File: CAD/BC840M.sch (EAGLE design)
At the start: 34 parts, among them J1 SM02B-SRSS-TB(LF)(SN), U2 BC840M, U3 LP5907MFX-3.3/NOPB, U4 LP5907MFX-3.3/NOPB, U5 ADS131M08IPBS, X1 ABM3B-8.000MHZ-B2-T, X2 FC-12M

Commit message: updated
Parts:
- removed JP4, JP5: (no value), pinhead+:PINHD-2X10SMT
- added C16, C17, C20, C21, C24, C25, C28, C29: 0.1pF, standardparts:CAPACITOR.0603
- added JP2, JP3: (no value), pinhead+:PINHD-2X10SMT
- added R10, R11, R12, R13, R14, R15, R16, R17, R18, R19, R20, R21, R6, R7, R8, R9: 1GOhm, standardparts:RESISTOR.0603
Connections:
- removed net N$2: U2.H4/VSS, U2.H5/VSS, U2.H6/VSS, U2.H7/VSS
- removed net N$3: U2.F5/VDD
- removed net N$4: U2.G4/VSS, U2.G5/VSS, U2.G6/VSS
- removed net N$46: U2.F7/P001
- removed net N$47: U2.F6/P000
- removed net N$5: U2.G0/VSS
- removed net N$8: U2.A5/D-
- removed net N$9: U2.A4/D+
- new net 0NIN: C16.2, R8.2, U5.AN0N
- new net 0PIN: C16.1, R6.2, U5.AN0P
- new net 1NIN: C17.2, R9.2, U5.AN1N
- new net 1PIN: C17.1, R7.2, U5.AN1P
- new net 2NIN: C20.2, R12.2, U5.AIN2N
- new net 2PIN: C20.1, R10.2, U5.AIN2P
- new net 3NIN: C21.2, R13.2, U5.AIN3N
- new net 3PIN: C21.1, R11.2, U5.AIN3P
- new net 4NIN: C24.2, R16.2, U5.AIN4N
- new net 4PIN: C24.1, R14.2, U5.AIN4P
- new net 5NIN: C25.2, R17.2, U5.AIN5N
- new net 5PIN: C25.1, R15.2, U5.AIN5P
- new net 6NIN: C28.2, R20.2, U5.AIN6N
- new net 6PIN: C28.1, R18.2, U5.AIN6P
- new net 7NIN: C29.2, R21.2, U5.AIN7N
- new net 7PIN: C29.1, R19.2, U5.AIN7P
- net 0N: now also JP1.2, R8.1; no longer U5.AN0N
- net 0P: now also JP1.1, R6.1; no longer U5.AN0P
- net 1N: now also JP1.4, R9.1; no longer U5.AN1N
- net 1P: now also JP1.3, R7.1; no longer U5.AN1P
- net 2N: now also JP1.6, R12.1; no longer U5.AIN2N
- net 2P: now also JP1.5, R10.1; no longer U5.AIN2P
- net 3N: now also JP1.8, R13.1; no longer U5.AIN3N
- net 3P: now also JP1.7, R11.1; no longer U5.AIN3P
- net 4N: now also JP1.10, R16.1; no longer U5.AIN4N
- net 4P: now also JP1.9, R14.1; no longer U5.AIN4P
- net 5N: now also JP1.12, R17.1; no longer U5.AIN5N
- net 5P: now also JP1.11, R15.1; no longer U5.AIN5P
- net 6N: now also JP1.14, R20.1; no longer U5.AIN6N
- net 6P: now also JP1.13, R18.1; no longer U5.AIN6P
- net 7N: now also JP1.16, R21.1; no longer U5.AIN7N
- net 7P: now also JP1.15, R19.1; no longer U5.AIN7P
- net D+: now also U2.A4/D+
- net D-: now also U2.A5/D-
- net GND: now also U2.G0/VSS, U2.G4/VSS, U2.G5/VSS, U2.G6/VSS, U2.H4/VSS, U2.H5/VSS, U2.H6/VSS, U2.H7/VSS
- net VDD: now also U2.F5/VDD
- net XTAL1_1: now also U2.F6/P000
- net XTAL2_1: now also U2.F7/P001
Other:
- note added: "Battery Charger/Switcher System (See BQ2407X datasheet)"
- note removed: "Battery Charger/Switcher System (See LOLIN32 Schematic)"

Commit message: updated
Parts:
- C16, C17, C20, C21, C24, C25, C28, C29: value 0.1pF -> 10pF
- R10, R11, R12, R13, R14, R15, R16, R17, R18, R19, R20, R21, R6, R7, R8, R9: value 1GOhm -> 10MOhm
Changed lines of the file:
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@@
 <part name="R5" library="standardparts" deviceset="RESISTOR" device=".0201" value="3.3kΩ"/>
 <part name="SUPPLY1" library="supply2" library_urn="urn:adsk.eagle:library:372" deviceset="GND" device=""/>
-<part name="C16" library="standardparts" deviceset="CAPACITOR" device=".0603" value="0.1pF"/>
-<part name="R6" library="standardparts" deviceset="RESISTOR" device=".0603" value="1GOhm"/>
-<part name="C17" library="standardparts" deviceset="CAPACITOR" device=".0603" value="0.1pF"/>
-<part name="R7" library="standardparts" deviceset="RESISTOR" device=".0603" value="1GOhm"/>
-<part name="R8" library="standardparts" deviceset="RESISTOR" device=".0603" value="1GOhm"/>
-<part name="R9" library="standardparts" deviceset="RESISTOR" device=".0603" value="1GOhm"/>
-<part name="C20" library="standardparts" deviceset="CAPACITOR" device=".0603" value="0.1pF"/>
-<part name="R10" library="standardparts" deviceset="RESISTOR" device=".0603" value="1GOhm"/>
-<part name="C21" library="standardparts" deviceset="CAPACITOR" device=".0603" value="0.1pF"/>
-<part name="R11" library="standardparts" deviceset="RESISTOR" device=".0603" value="1GOhm"/>
-<part name="R12" library="standardparts" deviceset="RESISTOR" device=".0603" value="1GOhm"/>
-<part name="R13" library="standardparts" deviceset="RESISTOR" device=".0603" value="1GOhm"/>
-<part name="C24" library="standardparts" deviceset="CAPACITOR" device=".0603" value="0.1pF"/>
-<part name="R14" library="standardparts" deviceset="RESISTOR" device=".0603" value="1GOhm"/>
-<part name="C25" library="standardparts" deviceset="CAPACITOR" device=".0603" value="0.1pF"/>
-<part name="R15" library="standardparts" deviceset="RESISTOR" device=".0603" value="1GOhm"/>
-<part name="R16" library="standardparts" deviceset="RESISTOR" device=".0603" value="1GOhm"/>
-<part name="R17" library="standardparts" deviceset="RESISTOR" device=".0603" value="1GOhm"/>
-<part name="C28" library="standardparts" deviceset="CAPACITOR" device=".0603" value="0.1pF"/>
-<part name="R18" library="standardparts" deviceset="RESISTOR" device=".0603" value="1GOhm"/>
-<part name="C29" library="standardparts" deviceset="CAPACITOR" device=".0603" value="0.1pF"/>
-<part name="R19" library="standardparts" deviceset="RESISTOR" device=".0603" value="1GOhm"/>
-<part name="R20" library="standardparts" deviceset="RESISTOR" device=".0603" value="1GOhm"/>
-<part name="R21" library="standardparts" deviceset="RESISTOR" device=".0603" value="1GOhm"/>
+<part name="C16" library="standardparts" deviceset="CAPACITOR" device=".0603" value="10pF"/>
+<part name="R6" library="standardparts" deviceset="RESISTOR" device=".0603" value="10MOhm"/>
+<part name="C17" library="standardparts" deviceset="CAPACITOR" device=".0603" value="10pF"/>
+<part name="R7" library="standardparts" deviceset="RESISTOR" device=".0603" value="10MOhm"/>
+<part name="R8" library="standardparts" deviceset="RESISTOR" device=".0603" value="10MOhm"/>
+<part name="R9" library="standardparts" deviceset="RESISTOR" device=".0603" value="10MOhm"/>
+<part name="C20" library="standardparts" deviceset="CAPACITOR" device=".0603" value="10pF"/>
+<part name="R10" library="standardparts" deviceset="RESISTOR" device=".0603" value="10MOhm"/>
+<part name="C21" library="standardparts" deviceset="CAPACITOR" device=".0603" value="10pF"/>
+<part name="R11" library="standardparts" deviceset="RESISTOR" device=".0603" value="10MOhm"/>
+<part name="R12" library="standardparts" deviceset="RESISTOR" device=".0603" value="10MOhm"/>
+<part name="R13" library="standardparts" deviceset="RESISTOR" device=".0603" value="10MOhm"/>
+<part name="C24" library="standardparts" deviceset="CAPACITOR" device=".0603" value="10pF"/>
+<part name="R14" library="standardparts" deviceset="RESISTOR" device=".0603" value="10MOhm"/>
+<part name="C25" library="standardparts" deviceset="CAPACITOR" device=".0603" value="10pF"/>
+<part name="R15" library="standardparts" deviceset="RESISTOR" device=".0603" value="10MOhm"/>
+<part name="R16" library="standardparts" deviceset="RESISTOR" device=".0603" value="10MOhm"/>
+<part name="R17" library="standardparts" deviceset="RESISTOR" device=".0603" value="10MOhm"/>
+<part name="C28" library="standardparts" deviceset="CAPACITOR" device=".0603" value="10pF"/>
+<part name="R18" library="standardparts" deviceset="RESISTOR" device=".0603" value="10MOhm"/>
+<part name="C29" library="standardparts" deviceset="CAPACITOR" device=".0603" value="10pF"/>
+<part name="R19" library="standardparts" deviceset="RESISTOR" device=".0603" value="10MOhm"/>
+<part name="R20" library="standardparts" deviceset="RESISTOR" device=".0603" value="10MOhm"/>
+<part name="R21" library="standardparts" deviceset="RESISTOR" device=".0603" value="10MOhm"/>
 <part name="SUPPLY22" library="supply2" library_urn="urn:adsk.eagle:library:372" deviceset="GND" device=""/>
 <part name="SUPPLY23" library="supply2" library_urn="urn:adsk.eagle:library:372" deviceset="GND" device=""/>

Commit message: i/o prerouting
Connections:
- net N$10 renamed SWDIO
- net N$11 renamed P104
- net N$12 renamed P101
- net N$13 renamed P25
- net N$14 renamed P19
- net N$15 renamed P17
- net N$16 renamed P22
- net N$17 renamed P15
- net N$18 renamed RESET
- net N$19 renamed VBUS
- net N$20 renamed P7
- net N$21 renamed P12
- net N$22 renamed P107
- net N$23 renamed SWDCLK
- net N$24 renamed P20
- net N$25 renamed P21
- net N$26 renamed P14
- net N$27 renamed P108
- net N$28 renamed P109
- net N$29 renamed P8
- net N$30 renamed P100
- net N$31 renamed P105
- net N$32 renamed P9
- net N$33 renamed P16
- net N$34 renamed P13
- net N$35 renamed P11
- net N$36 renamed P27
- net N$37 renamed P6
- net N$38 renamed P103
- net N$39 renamed P106
- net N$40 renamed P10
- net N$41 renamed P115
- net N$42 renamed P29
- net N$43 renamed P31
- net N$44 renamed P26
- net N$45 renamed P4
- net N$49 renamed P2
- net N$50 renamed P112
- net N$51 renamed P102
- net N$52 renamed P24
- net N$53 renamed P23
- net N$54 renamed P5
- net N$55 renamed P113
- net N$56 renamed P111
- net N$57 renamed P30
- net N$58 renamed P114
- net N$59 renamed P110
- net N$6 renamed VDDH
- net N$60 renamed P28
- net N$61 renamed P3
- net N$7 renamed DCCH

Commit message: latest
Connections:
- net N$63 renamed CE
- net N$68 renamed EN1
- net N$69 renamed EN2
- net N$72 renamed TD
- net N$74 renamed TS
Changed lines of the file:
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@@
 <grid distance="1" unitdist="mil" unit="mil" style="lines" multiple="1" display="no" altdistance="0.01" altunitdist="inch" altunit="inch"/>
 <layers>
-<layer number="1" name="Top" color="4" fill="1" visible="yes" active="no"/>
-<layer number="2" name="Route2" color="16" fill="1" visible="yes" active="no"/>
-<layer number="3" name="Route3" color="17" fill="1" visible="yes" active="no"/>
-<layer number="4" name="Route4" color="18" fill="1" visible="yes" active="no"/>
-<layer number="5" name="Route5" color="19" fill="1" visible="yes" active="no"/>
-<layer number="6" name="Route6" color="25" fill="1" visible="yes" active="no"/>
-<layer number="7" name="Route7" color="26" fill="1" visible="yes" active="no"/>
-<layer number="8" name="Route8" color="27" fill="1" visible="yes" active="no"/>
-<layer number="9" name="Route9" color="28" fill="1" visible="yes" active="no"/>
-<layer number="10" name="Route10" color="29" fill="1" visible="yes" active="no"/>
-<layer number="11" name="Route11" color="30" fill="1" visible="yes" active="no"/>
-<layer number="12" name="Route12" color="20" fill="1" visible="yes" active="no"/>
-<layer number="13" name="Route13" color="21" fill="1" visible="yes" active="no"/>
-<layer number="14" name="Route14" color="22" fill="1" visible="yes" active="no"/>
-<layer number="15" name="Route15" color="23" fill="1" visible="yes" active="no"/>
-<layer number="16" name="Bottom" color="1" fill="1" visible="yes" active="no"/>
-<layer number="17" name="Pads" color="2" fill="1" visible="yes" active="no"/>
-<layer number="18" name="Vias" color="2" fill="1" visible="yes" active="no"/>
-<layer number="19" name="Unrouted" color="6" fill="1" visible="yes" active="no"/>
-<layer number="20" name="Dimension" color="24" fill="1" visible="yes" active="no"/>
-<layer number="21" name="tPlace" color="7" fill="1" visible="yes" active="no"/>
-<layer number="22" name="bPlace" color="7" fill="1" visible="yes" active="no"/>
-<layer number="23" name="tOrigins" color="15" fill="1" visible="yes" active="no"/>
-<layer number="24" name="bOrigins" color="15" fill="1" visible="yes" active="no"/>
-<layer number="25" name="tNames" color="7" fill="1" visible="yes" active="no"/>
-<layer number="26" name="bNames" color="7" fill="1" visible="yes" active="no"/>
-<layer number="27" name="tValues" color="7" fill="1" visible="yes" active="no"/>
-<layer number="28" name="bValues" color="7" fill="1" visible="yes" active="no"/>
+<layer number="1" name="Top" color="4" fill="1" visible="no" active="no"/>
+<layer number="2" name="Route2" color="16" fill="1" visible="no" active="no"/>
+<layer number="3" name="Route3" color="17" fill="1" visible="no" active="no"/>
+<layer number="4" name="Route4" color="18" fill="1" visible="no" active="no"/>
+<layer number="5" name="Route5" color="19" fill="1" visible="no" active="no"/>
+<layer number="6" name="Route6" color="25" fill="1" visible="no" active="no"/>
+<layer number="7" name="Route7" color="26" fill="1" visible="no" active="no"/>
+<layer number="8" name="Route8" color="27" fill="1" visible="no" active="no"/>
+<layer number="9" name="Route9" color="28" fill="1" visible="no" active="no"/>
+<layer number="10" name="Route10" color="29" fill="1" visible="no" active="no"/>
+<layer number="11" name="Route11" color="30" fill="1" visible="no" active="no"/>
+<layer number="12" name="Route12" color="20" fill="1" visible="no" active="no"/>
+<layer number="13" name="Route13" color="21" fill="1" visible="no" active="no"/>
+<layer number="14" name="Route14" color="22" fill="1" visible="no" active="no"/>
+<layer number="15" name="Route15" color="23" fill="1" visible="no" active="no"/>
+<layer number="16" name="Bottom" color="1" fill="1" visible="no" active="no"/>
+<layer number="17" name="Pads" color="2" fill="1" visible="no" active="no"/>
+<layer number="18" name="Vias" color="2" fill="1" visible="no" active="no"/>
+<layer number="19" name="Unrouted" color="6" fill="1" visible="no" active="no"/>
+<layer number="20" name="Dimension" color="24" fill="1" visible="no" active="no"/>
+<layer number="21" name="tPlace" color="7" fill="1" visible="no" active="no"/>
+<layer number="22" name="bPlace" color="7" fill="1" visible="no" active="no"/>
+<layer number="23" name="tOrigins" color="15" fill="1" visible="no" active="no"/>
+<layer number="24" name="bOrigins" color="15" fill="1" visible="no" active="no"/>
+<layer number="25" name="tNames" color="7" fill="1" visible="no" active="no"/>
+<layer number="26" name="bNames" color="7" fill="1" visible="no" active="no"/>
+<layer number="27" name="tValues" color="7" fill="1" visible="no" active="no"/>
+<layer number="28" name="bValues" color="7" fill="1" visible="no" active="no"/>
 <layer number="29" name="tStop" color="7" fill="3" visible="no" active="no"/>
 <layer number="30" name="bStop" color="7" fill="6" visible="no" active="no"/>
@@
 <layer number="35" name="tGlue" color="7" fill="4" visible="no" active="no"/>
 <layer number="36" name="bGlue" color="7" fill="5" visible="no" active="no"/>
-<layer number="37" name="tTest" color="7" fill="1" visible="yes" active="no"/>
-<layer number="38" name="bTest" color="7" fill="1" visible="yes" active="no"/>
+<layer number="37" name="tTest" color="7" fill="1" visible="no" active="no"/>
+<layer number="38" name="bTest" color="7" fill="1" visible="no" active="no"/>
 <layer number="39" name="tKeepout" color="4" fill="11" visible="no" active="no"/>
 <layer number="40" name="bKeepout" color="1" fill="11" visible="no" active="no"/>
@@
 <layer number="44" name="Drills" color="7" fill="1" visible="no" active="no"/>
 <layer number="45" name="Holes" color="7" fill="1" visible="no" active="no"/>
-<layer number="46" name="Milling" color="3" fill="1" visible="yes" active="no"/>
-<layer number="47" name="Measures" color="7" fill="1" visible="yes" active="no"/>
-<layer number="48" name="Document" color="7" fill="1" visible="yes" active="no"/>
-<layer number="49" name="Reference" color="7" fill="1" visible="yes" active="no"/>
-<layer number="50" name="dxf" color="7" fill="1" visible="yes" active="no"/>
-<layer number="51" name="tDocu" color="7" fill="1" visible="yes" active="no"/>
-<layer number="52" name="bDocu" color="7" fill="1" visible="yes" active="no"/>
-<layer number="53" name="tGND_GNDA" color="7" fill="9" visible="yes" active="no"/>
-<layer number="54" name="bGND_GNDA" color="1" fill="9" visible="yes" active="no"/>
-<layer number="56" name="wert" color="7" fill="1" visible="yes" active="no"/>
-<layer number="57" name="tCAD" color="7" fill="1" visible="yes" active="no"/>
-<layer number="59" name="tCarbon" color="7" fill="1" visible="yes" active="no"/>
-<layer number="60" name="bCarbon" color="7" fill="1" visible="yes" active="no"/>
+<layer number="46" name="Milling" color="3" fill="1" visible="no" active="no"/>
+<layer number="47" name="Measures" color="7" fill="1" visible="no" active="no"/>
+<layer number="48" name="Document" color="7" fill="1" visible="no" active="no"/>
+<layer number="49" name="Reference" color="7" fill="1" visible="no" active="no"/>
+<layer number="50" name="dxf" color="7" fill="1" visible="no" active="no"/>
+<layer number="51" name="tDocu" color="7" fill="1" visible="no" active="no"/>
+<layer number="52" name="bDocu" color="7" fill="1" visible="no" active="no"/>
+<layer number="53" name="tGND_GNDA" color="7" fill="9" visible="no" active="no"/>
+<layer number="54" name="bGND_GNDA" color="1" fill="9" visible="no" active="no"/>
+<layer number="56" name="wert" color="7" fill="1" visible="no" active="no"/>
+<layer number="57" name="tCAD" color="7" fill="1" visible="no" active="no"/>
+<layer number="59" name="tCarbon" color="7" fill="1" visible="no" active="no"/>
+<layer number="60" name="bCarbon" color="7" fill="1" visible="no" active="no"/>
 <layer number="88" name="SimResults" color="9" fill="1" visible="yes" active="yes"/>
 <layer number="89" name="SimProbes" color="9" fill="1" visible="yes" active="yes"/>
@@
 </segment>
 </net>
-<net name="N$63" class="0">
+<net name="CE" class="0">
 <segment>
 <pinref part="U$2" gate="G$1" pin="!CE"/>
 <wire x1="48.1584" y1="83.3628" x2="44.45" y2="83.3628" width="0.1524" layer="91"/>
+<label x="43.3578" y="84.0486" size="1.778" layer="95" rot="R180"/>
 </segment>
 </net>
@@
 </segment>
 </net>
-<net name="N$68" class="0">
+<net name="EN1" class="0">
 <segment>
 <pinref part="U$2" gate="G$1" pin="EN1"/>
 <wire x1="48.1584" y1="60.5028" x2="44.7548" y2="60.5028" width="0.1524" layer="91"/>
-</segment>
-</net>
-<net name="N$69" class="0">
+<label x="43.7896" y="61.4934" size="1.778" layer="95" rot="R180"/>
+</segment>
+</net>
+<net name="EN2" class="0">
 <segment>
 <pinref part="U$2" gate="G$1" pin="EN2"/>
 <wire x1="48.1584" y1="57.9628" x2="44.704" y2="57.9628" width="0.1524" layer="91"/>
 <wire x1="44.704" y1="57.9628" x2="44.704" y2="57.912" width="0.1524" layer="91"/>
-</segment>
-</net>
-<net name="N$72" class="0">
+<label x="43.8658" y="58.5978" size="1.778" layer="95" rot="R180"/>
+</segment>
+</net>
+<net name="TD" class="0">
 <segment>
 <pinref part="U$2" gate="G$1" pin="TD"/>
 <wire x1="48.1584" y1="42.7228" x2="44.8056" y2="42.7228" width="0.1524" layer="91"/>
 <wire x1="44.8056" y1="42.7228" x2="44.8056" y2="42.672" width="0.1524" layer="91"/>
-</segment>
-</net>
-<net name="N$74" class="0">
+<label x="43.8658" y="43.4594" size="1.778" layer="95" rot="R180"/>
+</segment>
+</net>
+<net name="TS" class="0">
 <segment>
 <pinref part="U$2" gate="G$1" pin="TS"/>
 <wire x1="48.1584" y1="32.5628" x2="44.7802" y2="32.5628" width="0.1524" layer="91"/>
-</segment>
-</net>
+<label x="44.1198" y="33.4264" size="1.778" layer="95" rot="R180"/>
+</segment>
+</net>

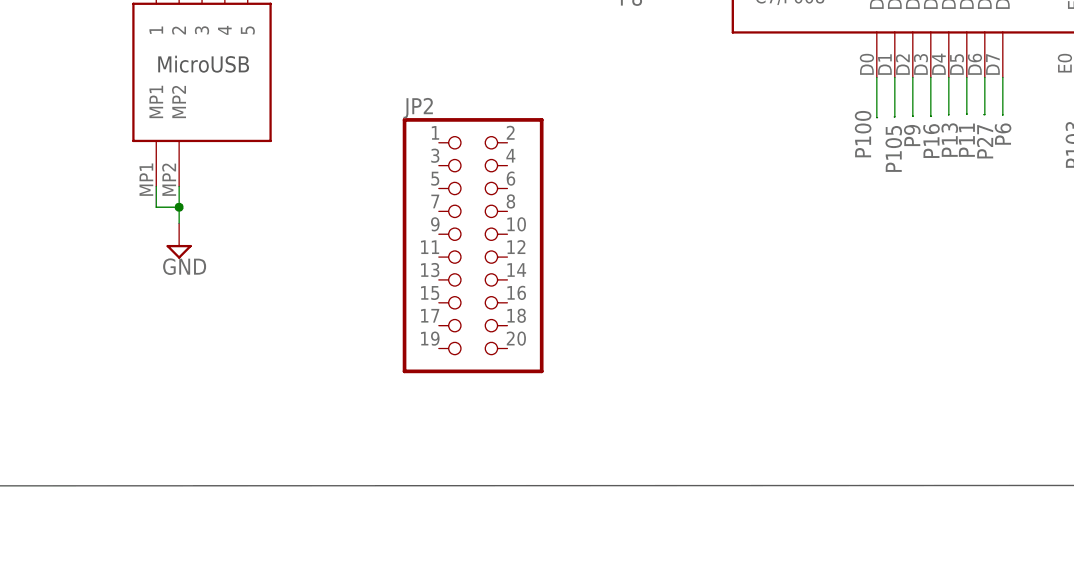
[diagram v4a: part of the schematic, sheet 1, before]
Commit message: grounding routed
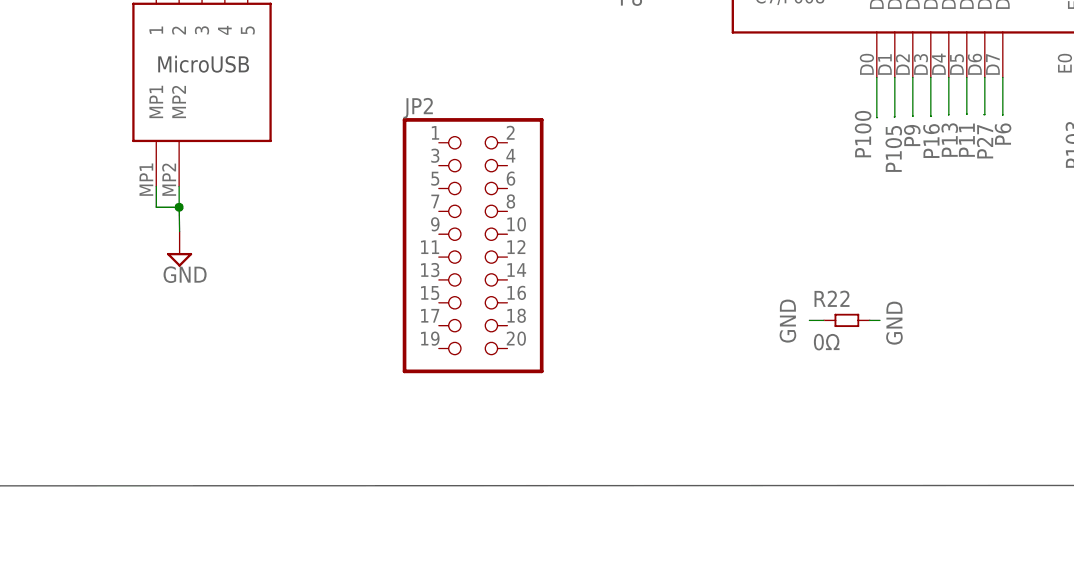
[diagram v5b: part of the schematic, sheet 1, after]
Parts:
- added R22: 0Ω, standardparts:RESISTOR.0603
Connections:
- net GND: now also R22.1, R22.2

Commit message: latest
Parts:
- added S1: CL-SB-12B-01T, CL-SB-12B-01T:CL-SB-12B-01T
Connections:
- new net VSWITCH: C11.2, S1.3, U$2.OUT@10
- net VIN: now also S1.2; no longer C11.2, U$2.OUT@10

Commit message: latest
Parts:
- removed LED1, LED2: (no value), adafruit:LEDCHIP-LED0603
- removed R5: 3.3kΩ, standardparts:RESISTOR.0201
- added R23: 348kΩ, standardparts:RESISTOR.0603
- added R24: 750kΩ, standardparts:RESISTOR.0603
- added R25: 0Ω, standardparts:RESISTOR.0805
- added SJ1: (no value), jumper:SJ
- R2: value 3.3kΩ -> 100kΩ
- R22: device standardparts:RESISTOR.0603 -> standardparts:RESISTOR.0805
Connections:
- removed net N$1: LED2.A, R2.1
- removed net N$62: LED1.A, R5.1
- removed net VBUS: U2.B5/VBUS
- net +5V: now also U2.B5/VBUS
- net AVDD: now also SJ1.2
- net BAT: now also R23.1
- net CHG: no longer R5.2
- net GND: now also R24.2; no longer LED1.C, LED2.C
- net P4: now also R23.2, R24.1
- net PGOOD: no longer R2.2
- net RESET: now also R2.1
- net VDD: now also R2.2, SJ1.1
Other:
- moved on the sheet: R2
